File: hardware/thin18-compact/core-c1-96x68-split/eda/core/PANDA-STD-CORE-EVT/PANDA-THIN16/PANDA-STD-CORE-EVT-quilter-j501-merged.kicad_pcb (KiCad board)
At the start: 4 copper layers, 96 x 68 mm, 155 parts, among them J201 U20405-01 USB2.0, J301 HC-HY-2AWT, J302 HC-1.0-3PWT NTC, J501 TF-122-CCP9 / microSD, J502 HC-1.0-2PWT BTL, J503 TC2030-IDC-NL / DEBUG, J601 HC-PBB40C-60DS-0.4V-1.5-02, J803 X05A10H06G, J804 X05A10H06G, Q907 NX3008NBK,215-JSM, Q908 NX3008NBK,215-JSM, SW201 TS-1186E-B-B, SW202 TS-1186E-B-B, U302 SD3078, U402 SGM2578SDYG/TR, U403 SGM2578SDYG/TR, U404 SGM2578SDYG/TR, U405 SGM2578SDYG/TR, U501 ESP32-S3-WROOM-1U-N16R8, U503 QMI8658A, U601 XL9535, U901 SGM41513YTQF24G/TR, U902 SGM62125AXG/TR, U903 CW2217BAAD, U904 NS4168, U905 SGM37601YTRL20G/TR, U906 SGM809B-TXN3LG/TR

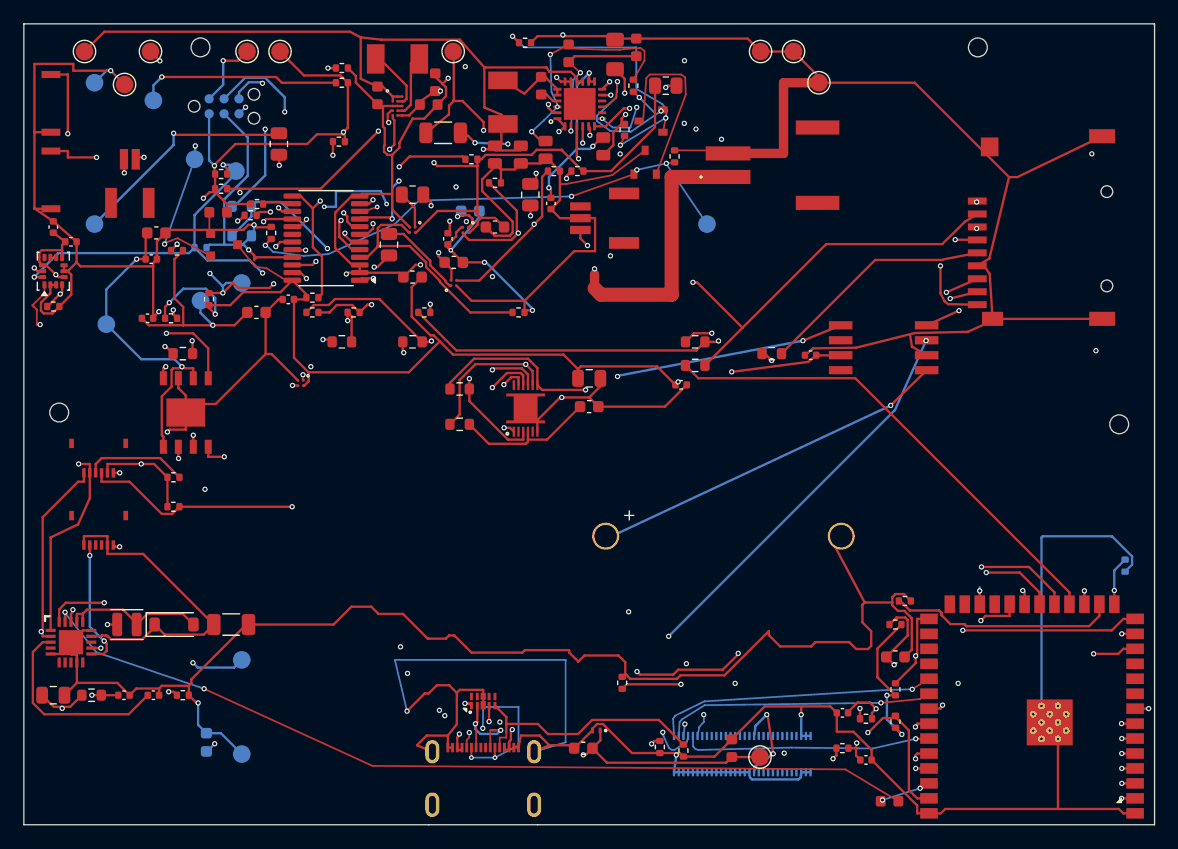
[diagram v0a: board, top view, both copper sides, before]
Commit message: hw: close reviewed via escapes and supervisor sourcing on develop
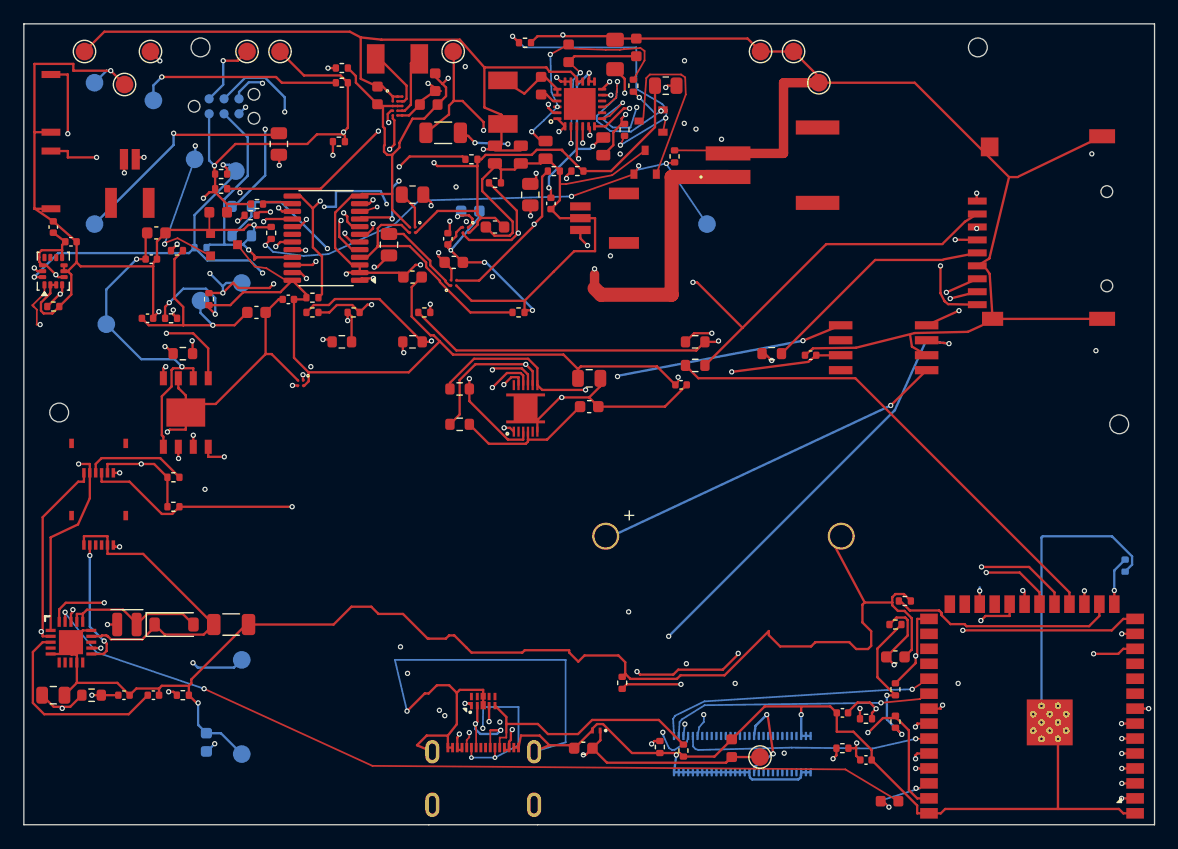
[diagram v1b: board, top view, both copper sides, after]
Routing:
- net BQ_INT: track 49.0 -> 53.5 mm
- net EXP_INT: track 174.3 -> 178.3 mm
- net 3V3_AON_SRC: track 24.8 -> 27.3 mm
- net HW_ARM_GPIO: track 3.53 -> 5.86 mm
- net SGM41513_PSEL: track 12.4 -> 14.5 mm
- net SDMMC_D2_CARD: track 82.3 -> 83.8 mm
- net 3V3_AON: track 345.2 -> 346.0 mm
- net FL_HWEN: track 157.0 -> 157.8 mm
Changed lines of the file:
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@@
 			)
 		)
-		(property "LCSC" ""
+		(property "LCSC" "C699619"
 			(at 0 0 0)
 			(layer "F.Fab")
@@
 	)
 	(via
-		(at 35.3674 5.7049)
+		(at 34.3174 5.0549)
 		(size 0.45)
 		(drill 0.25)
@@
 	)
 	(via
-		(at 49.1 8.05)
+		(at 50.85 6.7)
 		(size 0.4)
 		(drill 0.2)
@@
 (via (at 79.075 18.325) (size 0.45) (drill 0.25) (layers "F.Cu" "B.Cu") (net "3V3_SD"))
 (segment (start 80.95 17.245) (end 80.9 17.375) (width 0.2) (layer "F.Cu") (net "SDMMC_CMD_CARD"))
-(via (at 80.9 15.125) (size 0.45) (drill 0.25) (layers "F.Cu" "B.Cu") (net "SDMMC_D2_CARD"))
+(via (at 80.9 14.375) (size 0.45) (drill 0.25) (layers "F.Cu" "B.Cu") (net "SDMMC_D2_CARD"))
 (segment (start 80.95 18.345) (end 79.075 18.325) (width 0.2) (layer "F.Cu") (net "3V3_SD"))
 (segment (start 50.4045 29.9429) (end 50.4045 41.3) (width 0.2) (layer "In1.Cu") (net "I2C_SCL"))
@@
 (segment (start 76.6 26.9) (end 73.95 32.8) (width 0.2) (layer "B.Cu") (net "EXP_INT"))
 (segment (start 73.95 32.8) (end 54.75 52.0) (width 0.2) (layer "B.Cu") (net "EXP_INT"))
-(via (at 55.55 30.4) (size 0.45) (drill 0.25) (layers "F.Cu" "B.Cu") (net "3V3_AON"))
+(via (at 55.55 30.0) (size 0.45) (drill 0.25) (layers "F.Cu" "B.Cu") (net "3V3_AON"))
 (via (at 60.1 29.55) (size 0.45) (drill 0.25) (layers "F.Cu" "B.Cu") (net "3V3_AON"))
 (via (at 73.6 32.4) (size 0.45) (drill 0.25) (layers "F.Cu" "B.Cu") (net "RTC_VBACKUP"))
@@
 (via (at 79.4 24.35) (size 0.45) (drill 0.25) (layers "F.Cu" "B.Cu") (net "I2C_SDA"))
 (via (at 54.75 52.0) (size 0.45) (drill 0.25) (layers "F.Cu" "B.Cu") (net "EXP_INT"))
-(via (at 76.6 26.9) (size 0.45) (drill 0.25) (layers "F.Cu" "B.Cu") (net "EXP_INT"))
+(via (at 78.55 27.15) (size 0.45) (drill 0.25) (layers "F.Cu" "B.Cu") (net "EXP_INT"))
 (segment (start 46.45 8.7) (end 46.45 9.1) (width 0.15) (layer "F.Cu") (net "SGM41513_PSEL"))
 (segment (start 46.45 9.1) (end 46.65 4.75) (width 0.15) (layer "B.Cu") (net "SGM41513_PSEL"))
@@
 (segment (start 15.75 16.0) (end 15.75 17.4) (width 0.15) (layer "F.Cu") (net "GND"))
 (segment (start 15.855 17.8) (end 15.85 17.8) (width 0.15) (layer "F.Cu") (net "GND"))
-(via (at 46.45 9.1) (size 0.45) (drill 0.25) (layers "F.Cu" "B.Cu") (net "SGM41513_PSEL"))
+(via (at 46.45 10.15) (size 0.45) (drill 0.25) (layers "F.Cu" "B.Cu") (net "SGM41513_PSEL"))
 (via (at 47.25 4.15) (size 0.45) (drill 0.25) (layers "F.Cu" "B.Cu") (net "SGM41513_PSEL"))
 (via (at 44.7 2.6) (size 0.45) (drill 0.25) (layers "F.Cu" "B.Cu") (net "SGM41513_REGN"))
@@
 (via (at 54.5 8.0) (size 0.45) (drill 0.25) (layers "F.Cu" "B.Cu") (net "CHG_REQUEST"))
 (via (at 50.65 10.3) (size 0.45) (drill 0.25) (layers "F.Cu" "B.Cu") (net "CHG_REQUEST"))
-(via (at 76.1 64.9) (size 0.45) (drill 0.25) (layers "F.Cu" "B.Cu") (net "HW_ARM_GPIO"))
-(via (at 72.9 65.9) (size 0.45) (drill 0.25) (layers "F.Cu" "B.Cu") (net "HW_ARM_GPIO"))
+(via (at 75.75 64.9) (size 0.45) (drill 0.25) (layers "F.Cu" "B.Cu") (net "HW_ARM_GPIO"))
+(via (at 73.45 66.5) (size 0.45) (drill 0.25) (layers "F.Cu" "B.Cu") (net "HW_ARM_GPIO"))
 (via (at 15.3 56.45) (size 0.45) (drill 0.25) (layers "F.Cu" "B.Cu") (net "FL_HWEN"))
 (via (at 46.5 14.65) (size 0.45) (drill 0.25) (layers "F.Cu" "B.Cu") (net "FL_HWEN"))
 (via (at 54.55 11.85) (size 0.45) (drill 0.25) (layers "F.Cu" "B.Cu") (net "FL_HWEN"))
-(via (at 52.05 12.4) (size 0.45) (drill 0.25) (layers "F.Cu" "B.Cu") (net "FL_HWEN"))
+(via (at 52.2 12.05) (size 0.45) (drill 0.25) (layers "F.Cu" "B.Cu") (net "FL_HWEN"))
+(segment (start 55.55 30.4) (end 55.55 30.0) (width 0.2) (layer "In2.Cu") (net "3V3_AON"))
+(segment (start 80.9 15.125) (end 80.9 14.375) (width 0.2) (layer "In2.Cu") (net "SDMMC_D2_CARD"))
+(segment (start 49.1 8.05) (end 49.75 7.8) (width 0.15) (layer "F.Cu") (net "BQ_INT"))
+(segment (start 80.9 15.125) (end 80.9 14.375) (width 0.2) (layer "F.Cu") (net "SDMMC_D2_CARD"))
+(segment (start 46.45 9.1) (end 46.45 10.15) (width 0.15) (layer "F.Cu") (net "SGM41513_PSEL"))
+(segment (start 49.75 7.8) (end 50.85 6.7) (width 0.15) (layer "F.Cu") (net "BQ_INT"))
+(segment (start 76.1 64.9) (end 75.75 64.9) (width 0.15) (layer "F.Cu") (net "HW_ARM_GPIO"))
+(segment (start 46.45 9.1) (end 46.45 10.15) (width 0.15) (layer "B.Cu") (net "SGM41513_PSEL"))
+(segment (start 76.6 26.9) (end 78.55 27.15) (width 0.2) (layer "F.Cu") (net "EXP_INT"))
+(segment (start 55.55 30.4) (end 55.55 30.0) (width 0.15) (layer "F.Cu") (net "3V3_AON"))
+(segment (start 72.9 65.9) (end 73.45 66.5) (width 0.15) (layer "B.Cu") (net "HW_ARM_GPIO"))
+(segment (start 72.9 65.9) (end 73.45 66.5) (width 0.15) (layer "F.Cu") (net "HW_ARM_GPIO"))
+(segment (start 52.05 12.4) (end 52.2 12.05) (width 0.15) (layer "B.Cu") (net "FL_HWEN"))
+(segment (start 52.05 12.4) (end 52.2 12.05) (width 0.15) (layer "F.Cu") (net "FL_HWEN"))
+(segment (start 35.3674 5.7049) (end 34.3174 5.0549) (width 0.2) (layer "F.Cu") (net "3V3_AON_SRC"))
+(segment (start 76.6 26.9) (end 78.55 27.15) (width 0.2) (layer "B.Cu") (net "EXP_INT"))
+(segment (start 35.3674 5.7049) (end 34.3174 5.0549) (width 0.2) (layer "In2.Cu") (net "3V3_AON_SRC"))
+(segment (start 76.1 64.9) (end 75.75 64.9) (width 0.15) (layer "B.Cu") (net "HW_ARM_GPIO"))
+(segment (start 49.1 8.05) (end 50.85 6.7) (width 0.15) (layer "B.Cu") (net "BQ_INT"))
 )
